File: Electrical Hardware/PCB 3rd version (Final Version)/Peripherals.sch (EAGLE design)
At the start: 92 parts

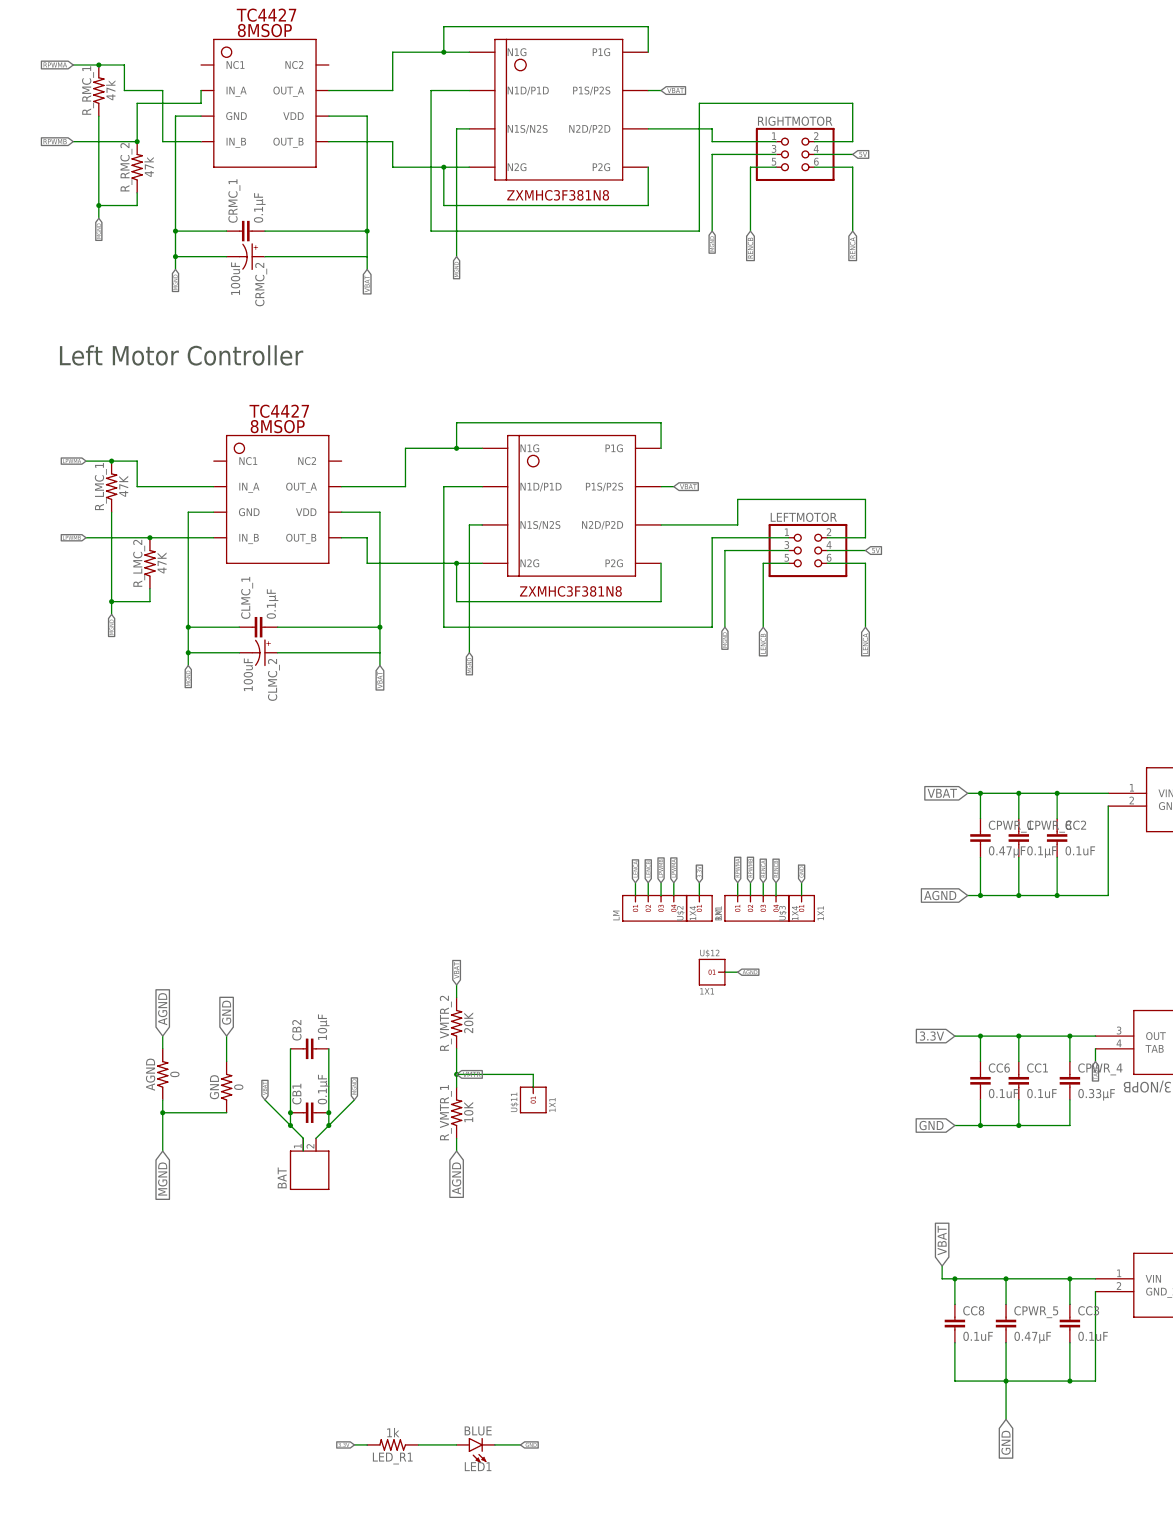
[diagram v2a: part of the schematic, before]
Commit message: Finshing PCB 3rd version Peripheral Board
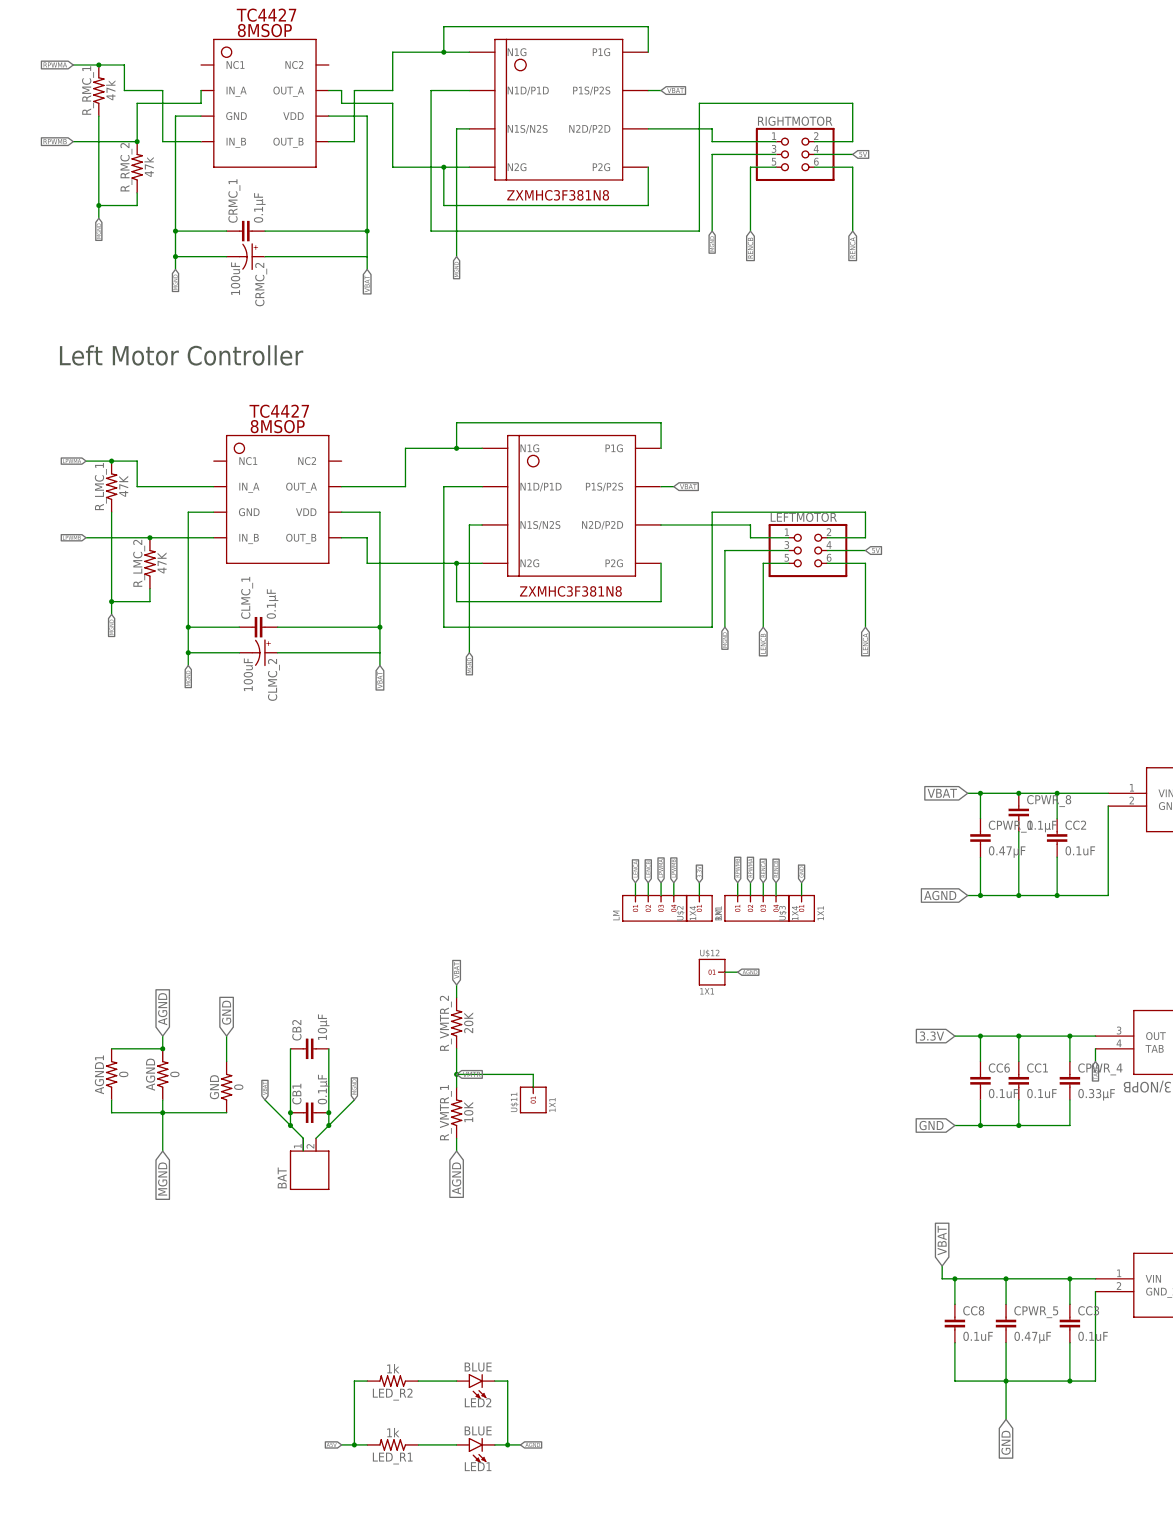
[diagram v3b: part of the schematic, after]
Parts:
- added AGND1: 0, SparkFun-Resistors:0.75OHM-0805-1/4W-1%
- added LED2: BLUE, SparkFun-LED:LED-BLUE1206
- added LED_R2: 1k, SparkFun-Resistors:0.75OHM-0805-1/4W-1%
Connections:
- removed net N$28: LEFTMOTOR.2, U$16.N2D/P2D
- new net N$10: LED2.A, LED_R2.1
- new net N$9: LEFTMOTOR.1, U$16.N2D/P2D
- net 3.3V: no longer LED_R1.2
- net A5V: now also LED_R1.2, LED_R2.2
- net AGND: now also AGND1.2, LED1.C, LED2.C
- net GND: no longer LED1.C
- net L: now also LEFTMOTOR.2; no longer LEFTMOTOR.1
- net LPWMA: now also LM.3; no longer LM.4
- net LPWMB: now also LM.4; no longer LM.3
- net MGND: now also AGND1.1
- net OUTA: now also U$17.OUT_B; no longer U$17.OUT_A
- net OUTB: now also U$17.OUT_A; no longer U$17.OUT_B
- net RPWMA: now also RM.2; no longer RM.1
- net RPWMB: now also RM.1; no longer RM.2
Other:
- moved on the sheet: CPWR_8
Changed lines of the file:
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@@
 <part name="U$11" library="headers(2mm)" deviceset="1X1" device=""/>
 <part name="U$12" library="headers(2mm)" deviceset="1X1" device=""/>
+<part name="AGND1" library="SparkFun-Resistors" library_urn="urn:adsk.eagle:library:532" deviceset="0.75OHM" device="-0805-1/4W-1%" value="0"/>
+<part name="LED_R2" library="SparkFun-Resistors" deviceset="0.75OHM" device="-0805-1/4W-1%" value="1k"/>
+<part name="LED2" library="SparkFun-LED" deviceset="LED-BLUE" device="1206" value="BLUE"/>
 </parts>
 <sheets>
@@
 <instance part="CB1" gate="G$1" x="68.58" y="-48.26" rot="R90"/>
 <instance part="CC5" gate="G$1" x="312.42" y="20.32" rot="R180"/>
-<instance part="CPWR_8" gate="G$1" x="208.28" y="5.08"/>
+<instance part="CPWR_8" gate="G$1" x="208.28" y="10.16"/>
 <instance part="CPWR_9" gate="G$1" x="289.56" y="-15.24" rot="R270"/>
 <instance part="CC6" gate="G$1" x="200.66" y="-43.18"/>
@@
 <instance part="U$11" gate="G$1" x="111.76" y="-45.72" rot="R90"/>
 <instance part="U$12" gate="G$1" x="147.32" y="-20.32"/>
+<instance part="AGND1" gate="G$1" x="27.94" y="-40.64" rot="R90"/>
+<instance part="LED_R2" gate="G$1" x="83.82" y="-101.6" rot="R180"/>
+<instance part="LED2" gate="G$1" x="99.06" y="-101.6" rot="R90"/>
 </instances>
 <busses>
@@
 </segment>
 <segment>
-<pinref part="LED1" gate="G$1" pin="C"/>
-<wire x1="104.14" y1="-114.3" x2="109.22" y2="-114.3" width="0.1524" layer="91"/>
-<label x="109.22" y="-114.3" size="0.8128" layer="95" xref="yes"/>
-</segment>
-<segment>
 <pinref part="U$3" gate="G$1" pin="1"/>
 <wire x1="165.1" y1="-5.08" x2="165.1" y2="-2.54" width="0.1524" layer="91"/>
@@
 <wire x1="93.98" y1="76.2" x2="93.98" y2="48.26" width="0.1524" layer="91"/>
 <wire x1="93.98" y1="48.26" x2="147.32" y2="48.26" width="0.1524" layer="91"/>
-<wire x1="147.32" y1="48.26" x2="147.32" y2="66.04" width="0.1524" layer="91"/>
-<pinref part="LEFTMOTOR" gate="A" pin="1"/>
-<wire x1="147.32" y1="66.04" x2="162.56" y2="66.04" width="0.1524" layer="91"/>
-</segment>
-</net>
-<net name="N$28" class="0">
-<segment>
-<pinref part="U$16" gate="G$1" pin="N2D/P2D"/>
-<wire x1="137.16" y1="68.58" x2="152.4" y2="68.58" width="0.1524" layer="91"/>
-<wire x1="152.4" y1="68.58" x2="152.4" y2="73.66" width="0.1524" layer="91"/>
-<wire x1="152.4" y1="73.66" x2="177.8" y2="73.66" width="0.1524" layer="91"/>
-<wire x1="177.8" y1="73.66" x2="177.8" y2="66.04" width="0.1524" layer="91"/>
+<wire x1="147.32" y1="48.26" x2="147.32" y2="71.12" width="0.1524" layer="91"/>
+<wire x1="147.32" y1="71.12" x2="177.8" y2="71.12" width="0.1524" layer="91"/>
+<wire x1="177.8" y1="71.12" x2="177.8" y2="66.04" width="0.1524" layer="91"/>
 <pinref part="LEFTMOTOR" gate="A" pin="2"/>
 <wire x1="177.8" y1="66.04" x2="170.18" y2="66.04" width="0.1524" layer="91"/>
@@
 <net name="OUTB" class="0">
 <segment>
-<wire x1="83.82" y1="144.78" x2="83.82" y2="139.7" width="0.1524" layer="91"/>
 <pinref part="U$18" gate="G$1" pin="N2G"/>
 <wire x1="83.82" y1="139.7" x2="93.98" y2="139.7" width="0.1524" layer="91"/>
@@
 <pinref part="U$18" gate="G$1" pin="P2G"/>
 <junction x="93.98" y="139.7"/>
-<pinref part="U$17" gate="G$1" pin="OUT_B"/>
-<wire x1="83.82" y1="144.78" x2="71.12" y2="144.78" width="0.1524" layer="91"/>
+<wire x1="83.82" y1="139.7" x2="83.82" y2="152.4" width="0.1524" layer="91"/>
+<wire x1="83.82" y1="152.4" x2="73.66" y2="152.4" width="0.1524" layer="91"/>
+<wire x1="73.66" y1="152.4" x2="73.66" y2="154.94" width="0.1524" layer="91"/>
+<pinref part="U$17" gate="G$1" pin="OUT_A"/>
+<wire x1="73.66" y1="154.94" x2="71.12" y2="154.94" width="0.1524" layer="91"/>
 </segment>
 </net>
@@
 <wire x1="134.62" y1="167.64" x2="134.62" y2="162.56" width="0.1524" layer="91"/>
 <junction x="93.98" y="162.56"/>
-<wire x1="71.12" y1="154.94" x2="83.82" y2="154.94" width="0.1524" layer="91"/>
-<pinref part="U$17" gate="G$1" pin="OUT_A"/>
+<wire x1="83.82" y1="154.94" x2="76.2" y2="154.94" width="0.1524" layer="91"/>
+<wire x1="76.2" y1="154.94" x2="76.2" y2="144.78" width="0.1524" layer="91"/>
+<pinref part="U$17" gate="G$1" pin="OUT_B"/>
+<wire x1="76.2" y1="144.78" x2="71.12" y2="144.78" width="0.1524" layer="91"/>
 </segment>
 </net>
@@
 <junction x="200.66" y="15.24"/>
 <pinref part="CPWR_8" gate="G$1" pin="1"/>
-<wire x1="208.28" y1="10.16" x2="208.28" y2="15.24" width="0.1524" layer="91"/>
 <junction x="208.28" y="15.24"/>
 </segment>
@@
 <net name="LPWMB" class="0">
 <segment>
-<pinref part="LM" gate="G$1" pin="3"/>
-<wire x1="137.16" y1="-5.08" x2="137.16" y2="-2.54" width="0.1524" layer="91"/>
-<label x="137.16" y="-2.54" size="0.8128" layer="95" rot="R90" xref="yes"/>
-</segment>
-<segment>
 <wire x1="22.86" y1="66.04" x2="35.56" y2="66.04" width="0.1524" layer="91"/>
 <pinref part="R_LMC_2" gate="G$1" pin="2"/>
@@
 <junction x="35.56" y="66.04"/>
 </segment>
-</net>
-<net name="LPWMA" class="0">
 <segment>
 <pinref part="LM" gate="G$1" pin="4"/>
@@
 <label x="139.7" y="-2.54" size="0.8128" layer="95" rot="R90" xref="yes"/>
 </segment>
+</net>
+<net name="LPWMA" class="0">
 <segment>
 <wire x1="33.02" y1="81.28" x2="27.94" y2="81.28" width="0.1524" layer="91"/>
@@
 <wire x1="33.02" y1="81.28" x2="33.02" y2="76.2" width="0.1524" layer="91"/>
 <wire x1="33.02" y1="76.2" x2="48.26" y2="76.2" width="0.1524" layer="91"/>
+</segment>
+<segment>
+<pinref part="LM" gate="G$1" pin="3"/>
+<wire x1="137.16" y1="-5.08" x2="137.16" y2="-2.54" width="0.1524" layer="91"/>
+<label x="137.16" y="-2.54" size="0.8128" layer="95" rot="R90" xref="yes"/>
 </segment>
 </net>
@@
 </segment>
 <segment>
-<pinref part="RM" gate="G$1" pin="1"/>
-<wire x1="152.4" y1="-5.08" x2="152.4" y2="-2.54" width="0.1524" layer="91"/>
-<label x="152.4" y="-2.54" size="0.8128" layer="95" rot="R90" xref="yes"/>
+<pinref part="RM" gate="G$1" pin="2"/>
+<wire x1="154.94" y1="-5.08" x2="154.94" y2="-2.54" width="0.1524" layer="91"/>
+<label x="154.94" y="-2.54" size="0.8128" layer="95" rot="R90" xref="yes"/>
 </segment>
 </net>
@@
 </segment>
 <segment>
-<pinref part="RM" gate="G$1" pin="2"/>
-<wire x1="154.94" y1="-5.08" x2="154.94" y2="-2.54" width="0.1524" layer="91"/>
-<label x="154.94" y="-2.54" size="0.8128" layer="95" rot="R90" xref="yes"/>
+<pinref part="RM" gate="G$1" pin="1"/>
+<wire x1="152.4" y1="-5.08" x2="152.4" y2="-2.54" width="0.1524" layer="91"/>
+<label x="152.4" y="-2.54" size="0.8128" layer="95" rot="R90" xref="yes"/>
 </segment>
 </net>
@@
 </segment>
 <segment>
-<pinref part="LED_R1" gate="G$1" pin="2"/>
-<wire x1="78.74" y1="-114.3" x2="76.2" y2="-114.3" width="0.1524" layer="91"/>
-<label x="76.2" y="-114.3" size="0.8128" layer="95" rot="R180" xref="yes"/>
-</segment>
-<segment>
 <pinref part="U$2" gate="G$1" pin="1"/>
 <wire x1="144.78" y1="-5.08" x2="144.78" y2="-2.54" width="0.1524" layer="91"/>
@@
 <wire x1="38.1" y1="-48.26" x2="50.8" y2="-48.26" width="0.1524" layer="91"/>
 <label x="38.1" y="-55.88" size="1.778" layer="95" rot="R270" xref="yes"/>
+<pinref part="AGND1" gate="G$1" pin="1"/>
+<wire x1="27.94" y1="-45.72" x2="27.94" y2="-48.26" width="0.1524" layer="91"/>
+<wire x1="27.94" y1="-48.26" x2="38.1" y2="-48.26" width="0.1524" layer="91"/>
 </segment>
 <segment>
@@
 <junction x="215.9" y="-5.08"/>
 <pinref part="CPWR_8" gate="G$1" pin="2"/>
-<wire x1="208.28" y1="2.54" x2="208.28" y2="-5.08" width="0.1524" layer="91"/>
+<wire x1="208.28" y1="7.62" x2="208.28" y2="-5.08" width="0.1524" layer="91"/>
 <junction x="208.28" y="-5.08"/>
 </segment>
@@
 <wire x1="38.1" y1="-35.56" x2="38.1" y2="-33.02" width="0.1524" layer="91"/>
 <label x="38.1" y="-33.02" size="1.778" layer="95" rot="R90" xref="yes"/>
+<pinref part="AGND1" gate="G$1" pin="2"/>
+<wire x1="27.94" y1="-35.56" x2="38.1" y2="-35.56" width="0.1524" layer="91"/>
+<junction x="38.1" y="-35.56"/>
 </segment>
 <segment>
@@
 <wire x1="149.86" y1="-20.32" x2="152.4" y2="-20.32" width="0.1524" layer="91"/>
 <label x="152.4" y="-20.32" size="0.8128" layer="95" xref="yes"/>
+</segment>
+<segment>
+<pinref part="LED1" gate="G$1" pin="C"/>
+<wire x1="104.14" y1="-114.3" x2="106.68" y2="-114.3" width="0.1524" layer="91"/>
+<label x="109.22" y="-114.3" size="0.8128" layer="95" xref="yes"/>
+<pinref part="LED2" gate="G$1" pin="C"/>
+<wire x1="106.68" y1="-114.3" x2="109.22" y2="-114.3" width="0.1524" layer="91"/>
+<wire x1="104.14" y1="-101.6" x2="106.68" y2="-101.6" width="0.1524" layer="91"/>
+<wire x1="106.68" y1="-101.6" x2="106.68" y2="-114.3" width="0.1524" layer="91"/>
+<junction x="106.68" y="-114.3"/>
 </segment>
 </net>
@@
 <wire x1="-93.98" y1="-38.1" x2="-93.98" y2="-30.48" width="0.1524" layer="91"/>
 </segment>
+<segment>
+<pinref part="LED_R1" gate="G$1" pin="2"/>
+<wire x1="78.74" y1="-114.3" x2="76.2" y2="-114.3" width="0.1524" layer="91"/>
+<label x="73.66" y="-114.3" size="0.8128" layer="95" rot="R180" xref="yes"/>
+<pinref part="LED_R2" gate="G$1" pin="2"/>
+<wire x1="76.2" y1="-114.3" x2="73.66" y2="-114.3" width="0.1524" layer="91"/>
+<wire x1="78.74" y1="-101.6" x2="76.2" y2="-101.6" width="0.1524" layer="91"/>
+<wire x1="76.2" y1="-101.6" x2="76.2" y2="-114.3" width="0.1524" layer="91"/>
+<junction x="76.2" y="-114.3"/>
+</segment>
 </net>
 <net name="N$1" class="0">
@@
 </segment>
 </net>
+<net name="N$9" class="0">
+<segment>
+<pinref part="U$16" gate="G$1" pin="N2D/P2D"/>
+<wire x1="137.16" y1="68.58" x2="154.94" y2="68.58" width="0.1524" layer="91"/>
+<wire x1="154.94" y1="68.58" x2="154.94" y2="66.04" width="0.1524" layer="91"/>
+<pinref part="LEFTMOTOR" gate="A" pin="1"/>
+<wire x1="154.94" y1="66.04" x2="162.56" y2="66.04" width="0.1524" layer="91"/>
+</segment>
+</net>
+<net name="N$10" class="0">
+<segment>
+<pinref part="LED_R2" gate="G$1" pin="1"/>
+<pinref part="LED2" gate="G$1" pin="A"/>
+<wire x1="96.52" y1="-101.6" x2="88.9" y2="-101.6" width="0.1524" layer="91"/>
+</segment>
+</net>
